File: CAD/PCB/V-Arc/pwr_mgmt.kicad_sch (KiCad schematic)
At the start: 39 parts, among them J1 USB_C_Receptacle_USB2.0_16P, J2 Conn_01x02, U1 BQ24072RGT, U2 MT3608, U3 MT3608, U4 MAX1044

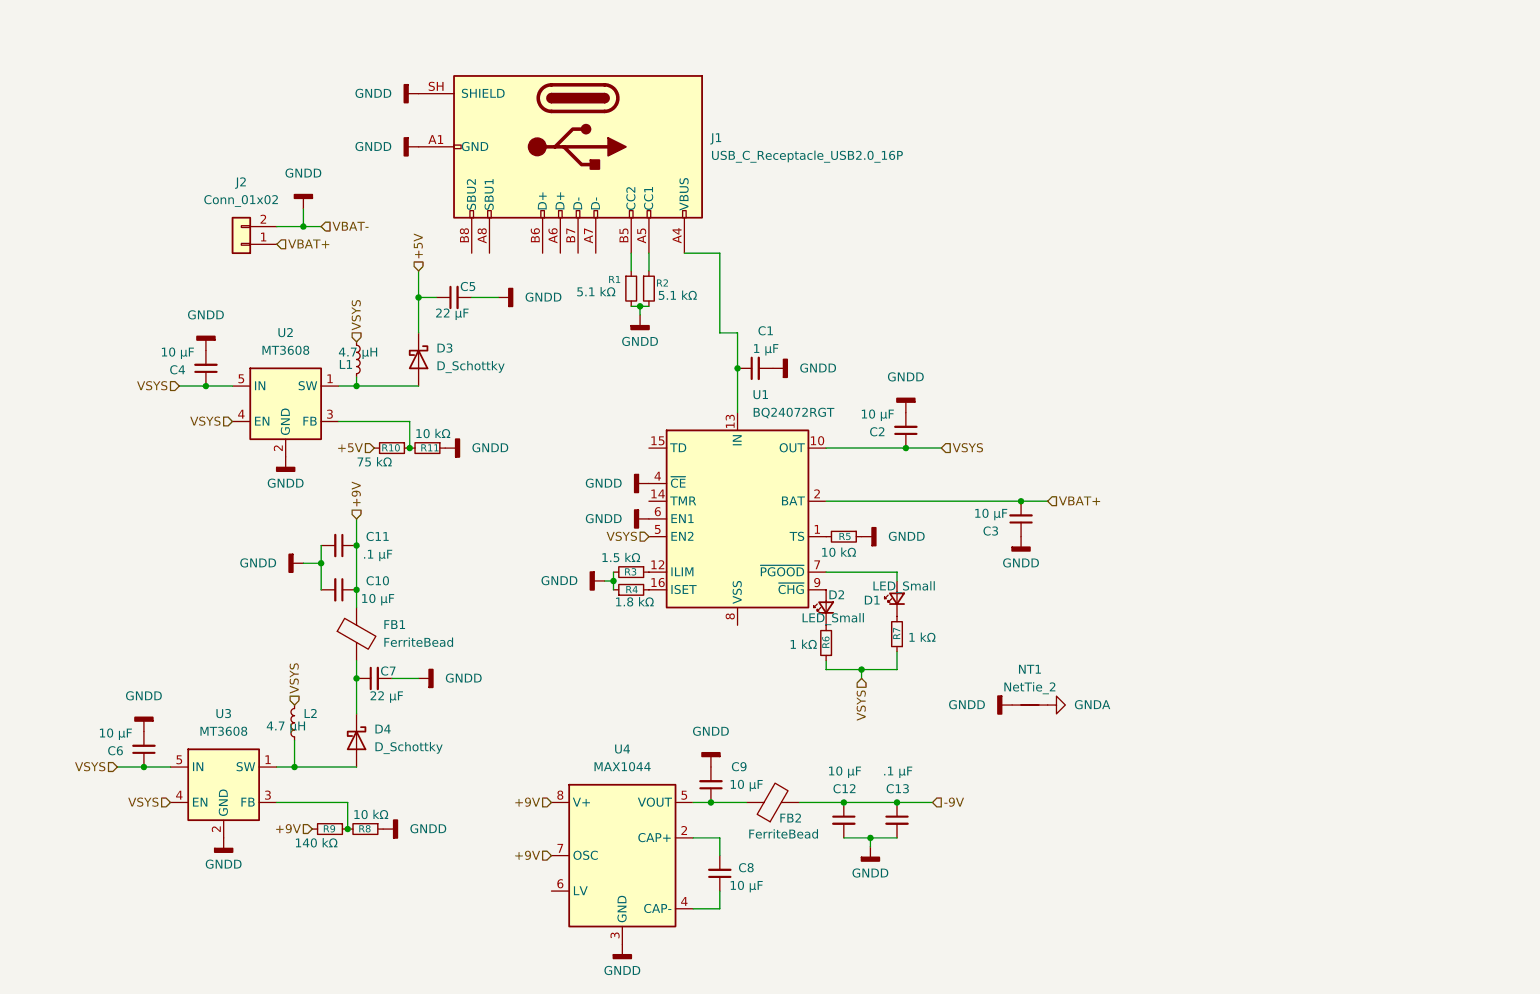
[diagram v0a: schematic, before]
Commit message: Added a sheet and organized
-Added XIAO ESP32 Core sheet
-Titled all sheets
-Added power switch to the power sheet
-Organized all sheets with text boxes
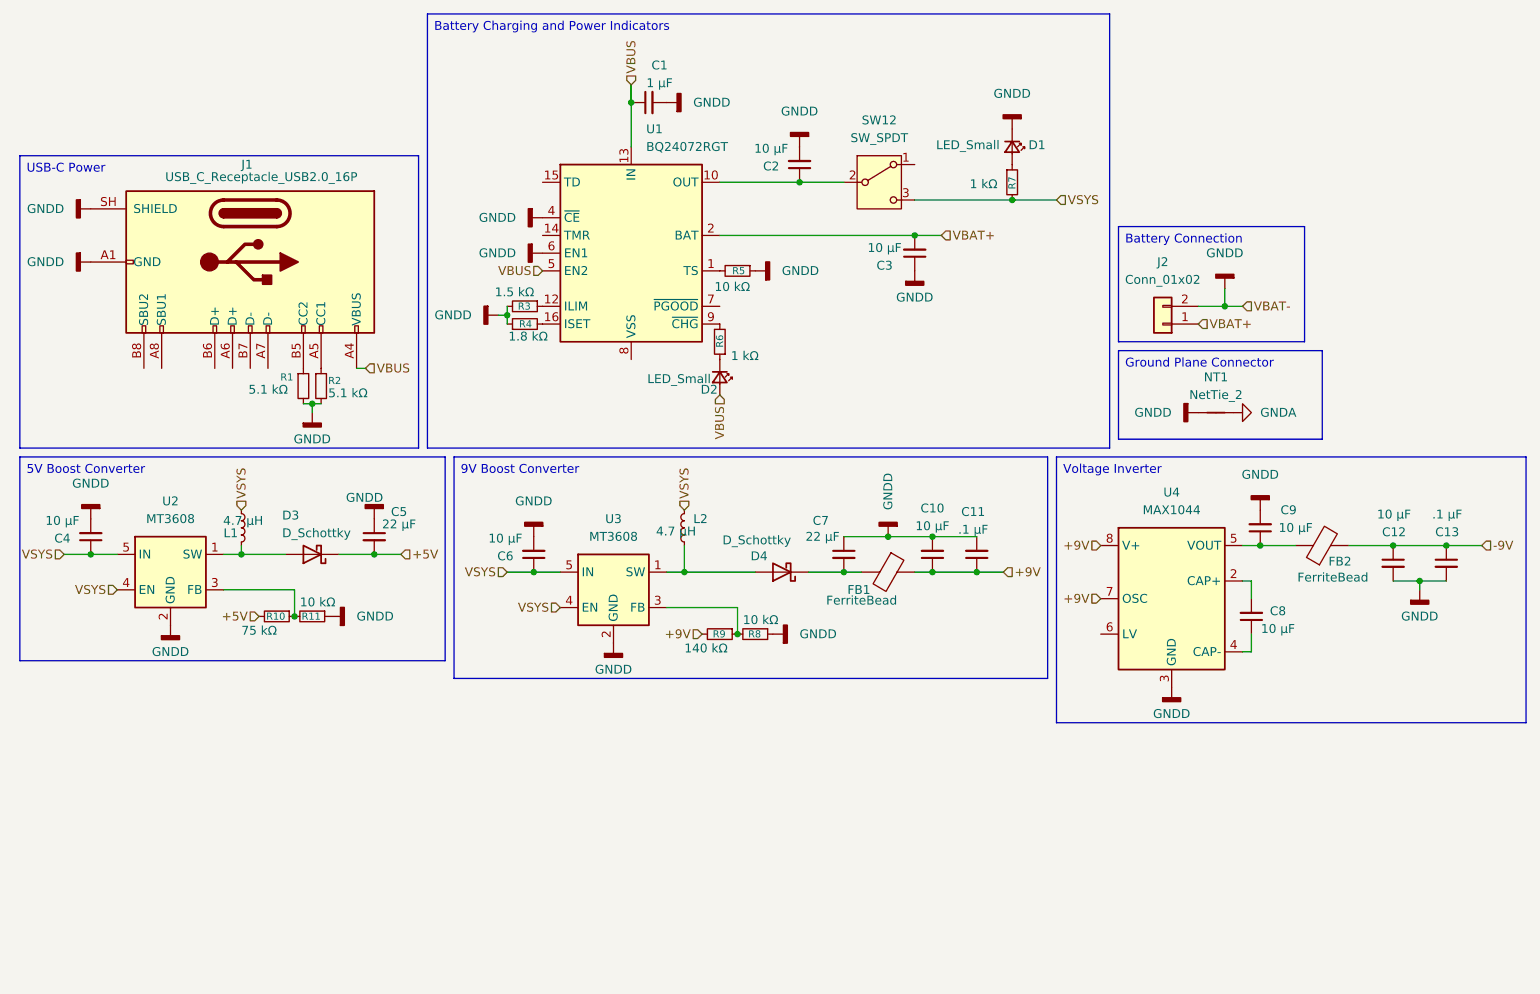
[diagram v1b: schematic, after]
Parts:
- added SW12: SW_SPDT, symbol Switch:SW_SPDT
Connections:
- net +5V: now also C5.2; no longer C5.1
- net GNDD: now also C5.1, C7.1, D1.1 (K); no longer C5.2, C7.2
- net VSYS: now also R7.2, SW12.3 (C); no longer C2.1, R6.1, R7.1, U1.10 (OUT), U1.11 (OUT), U1.5 (EN2)
- net VBUS: now reaches C1.1, J1.A4 (VBUS), J1.A9 (VBUS), J1.B4 (VBUS), J1.B9 (VBUS), U1.13 (IN)
- net VBUS: now also D2.2 (A), U1.5 (EN2)
- net at U1.7 (~{PGOOD}): no longer D1.2 (A)
- net at U1.9 (~{CHG}): now also R6.2; no longer D2.2 (A)
- net at D2.1 (K): now also R6.1; no longer R6.2
- net at D4.1 (K), FB1.2: now also C7.2; no longer C7.1
- new net: C2.1, SW12.2 (B), U1.10 (OUT), U1.11 (OUT)
- new net: D1.2 (A), R7.1
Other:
- title: (none) -> V-Arc Power Management
- moved on the sheet: C1, C10, C11, C12, C13, C2, C3, C4, C5, C6, C7, C8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
